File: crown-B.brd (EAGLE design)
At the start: 57.8 x 50.8 mm, 72 parts

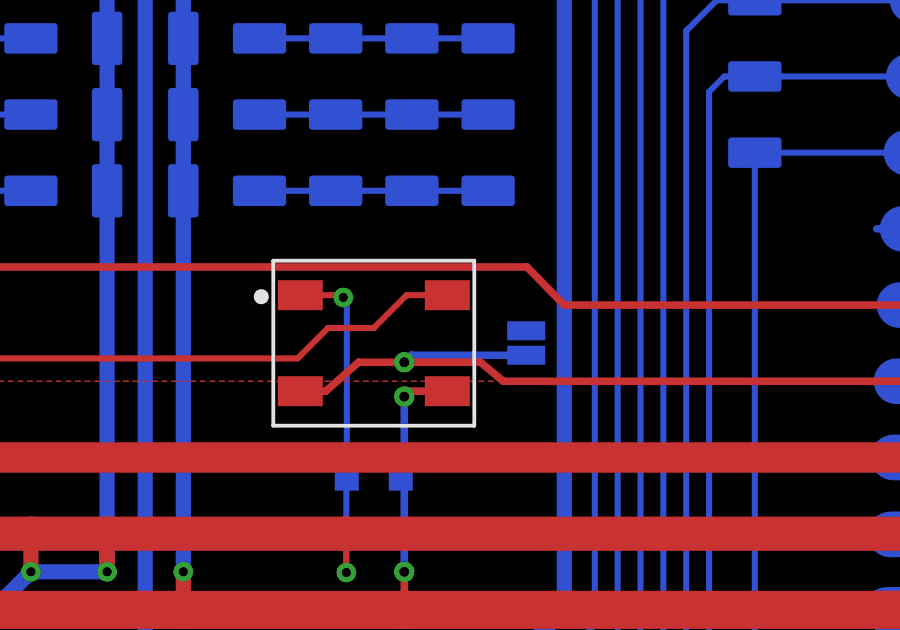
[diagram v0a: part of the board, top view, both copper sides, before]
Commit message: forgot a connection on skip-smd bits
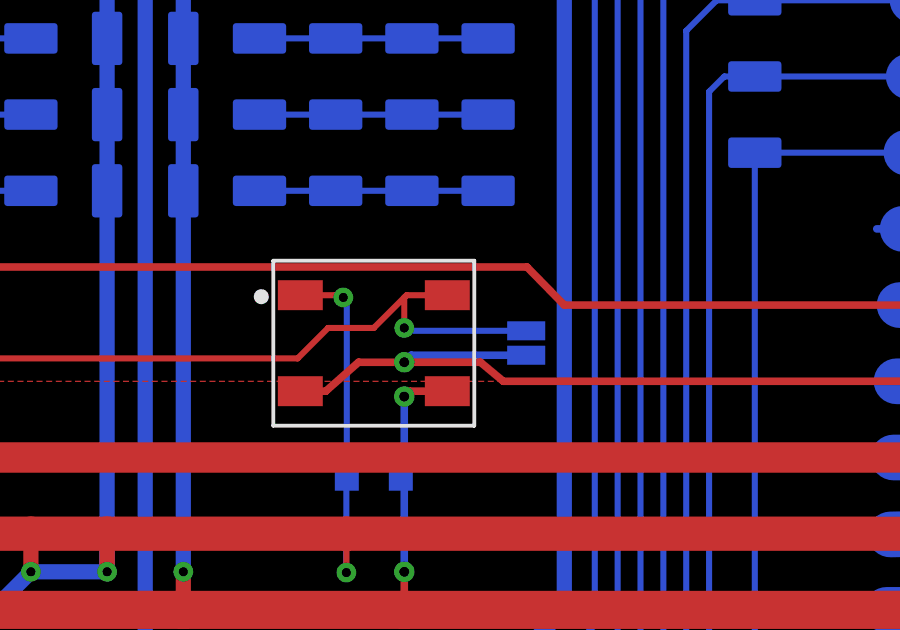
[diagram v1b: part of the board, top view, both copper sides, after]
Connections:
- net N$10: now also SKIP-SMD2.2
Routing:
- net N$10: track 28.2 -> 33.3 mm, vias 1 -> 2
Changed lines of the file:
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@@
 <grid distance="10" unitdist="mil" unit="mil" style="lines" multiple="5" display="yes" altdistance="1" altunitdist="mil" altunit="mil"/>
 <layers>
-<layer number="1" name="Top" color="4" fill="1" visible="no" active="yes"/>
-<layer number="16" name="Bottom" color="1" fill="1" visible="no" active="yes"/>
-<layer number="17" name="Pads" color="2" fill="1" visible="no" active="yes"/>
-<layer number="18" name="Vias" color="2" fill="1" visible="no" active="yes"/>
-<layer number="19" name="Unrouted" color="6" fill="1" visible="no" active="yes"/>
-<layer number="20" name="Dimension" color="15" fill="1" visible="no" active="yes"/>
-<layer number="21" name="tPlace" color="16" fill="1" visible="no" active="yes"/>
-<layer number="22" name="bPlace" color="14" fill="1" visible="no" active="yes"/>
-<layer number="23" name="tOrigins" color="15" fill="1" visible="no" active="yes"/>
-<layer number="24" name="bOrigins" color="15" fill="1" visible="no" active="yes"/>
+<layer number="1" name="Top" color="4" fill="1" visible="yes" active="yes"/>
+<layer number="16" name="Bottom" color="1" fill="1" visible="yes" active="yes"/>
+<layer number="17" name="Pads" color="2" fill="1" visible="yes" active="yes"/>
+<layer number="18" name="Vias" color="2" fill="1" visible="yes" active="yes"/>
+<layer number="19" name="Unrouted" color="6" fill="1" visible="yes" active="yes"/>
+<layer number="20" name="Dimension" color="15" fill="1" visible="yes" active="yes"/>
+<layer number="21" name="tPlace" color="16" fill="1" visible="yes" active="yes"/>
+<layer number="22" name="bPlace" color="14" fill="1" visible="yes" active="yes"/>
+<layer number="23" name="tOrigins" color="15" fill="1" visible="yes" active="yes"/>
+<layer number="24" name="bOrigins" color="15" fill="1" visible="yes" active="yes"/>
 <layer number="25" name="tNames" color="7" fill="1" visible="no" active="yes"/>
 <layer number="26" name="bNames" color="7" fill="1" visible="no" active="yes"/>
@@
 <layer number="28" name="bValues" color="7" fill="1" visible="no" active="yes"/>
 <layer number="29" name="tStop" color="7" fill="3" visible="yes" active="yes"/>
-<layer number="30" name="bStop" color="7" fill="6" visible="no" active="yes"/>
+<layer number="30" name="bStop" color="7" fill="6" visible="yes" active="yes"/>
 <layer number="31" name="tCream" color="7" fill="4" visible="no" active="yes"/>
 <layer number="32" name="bCream" color="7" fill="5" visible="no" active="yes"/>
@@
 <layer number="43" name="vRestrict" color="2" fill="10" visible="no" active="yes"/>
 <layer number="44" name="Drills" color="7" fill="1" visible="no" active="yes"/>
-<layer number="45" name="Holes" color="7" fill="1" visible="no" active="yes"/>
+<layer number="45" name="Holes" color="7" fill="1" visible="yes" active="yes"/>
 <layer number="46" name="Milling" color="3" fill="1" visible="no" active="yes"/>
 <layer number="47" name="Measures" color="7" fill="1" visible="no" active="yes"/>
@@
 <layer number="49" name="Reference" color="7" fill="1" visible="no" active="yes"/>
 <layer number="50" name="dxf" color="7" fill="1" visible="no" active="no"/>
-<layer number="51" name="tDocu" color="6" fill="1" visible="no" active="yes"/>
+<layer number="51" name="tDocu" color="6" fill="1" visible="yes" active="yes"/>
 <layer number="52" name="bDocu" color="7" fill="1" visible="no" active="yes"/>
 <layer number="53" name="tGND_GNDA" color="7" fill="9" visible="no" active="no"/>
@@
 <wire x1="35.56" y1="16.002" x2="36.576" y2="17.018" width="0.2032" layer="1"/>
 <wire x1="36.576" y1="17.018" x2="38.1" y2="17.018" width="0.2032" layer="1"/>
-<wire x1="38.1" y1="17.018" x2="39.192" y2="18.11" width="0.2032" layer="1"/>
+<wire x1="38.1" y1="17.018" x2="39.116" y2="18.034" width="0.2032" layer="1"/>
+<wire x1="39.116" y1="18.034" x2="39.192" y2="18.11" width="0.2032" layer="1"/>
 <wire x1="39.192" y1="18.11" x2="40.55" y2="18.11" width="0.2032" layer="1"/>
 <wire x1="24.892" y1="16.3631" x2="24.7849" y2="16.256" width="0.2032" layer="16"/>
@@
 <wire x1="21.336" y1="16.256" x2="21.082" y2="16.002" width="0.2032" layer="16"/>
 <via x="21.082" y="16.002" extent="1-16" drill="0.3048"/>
+<contactref element="SKIP-SMD2" pad="2"/>
+<wire x1="43.18" y1="16.9227" x2="39.2113" y2="16.9227" width="0.2032" layer="16"/>
+<wire x1="39.2113" y1="16.9227" x2="39.116" y2="17.018" width="0.2032" layer="16"/>
+<via x="39.116" y="17.018" extent="1-16" drill="0.3048"/>
+<wire x1="39.116" y1="17.018" x2="39.116" y2="18.034" width="0.2032" layer="1"/>
 </signal>
 <signal name="A0">

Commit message: fixed incorrect resistor value
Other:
- board text added: "PIXEL LINE TERMINATION (500 OHM RES)"
- board text removed: "PIXEL LINE TERMINATION (150 OHM RES)"
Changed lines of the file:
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@@
 <text x="12.954" y="16.51" size="0.762" layer="22" font="vector" ratio="15" rot="MR90" align="bottom-center">PIXEL LINE
 TERMINATION
-(150 OHM RES)</text>
+(500 OHM RES)</text>
 <text x="4.572" y="7.62" size="0.762" layer="22" font="vector" ratio="15" rot="MR0" align="center-right">GND</text>
 <text x="4.572" y="5.08" size="0.762" layer="22" font="vector" ratio="15" rot="MR0" align="center-right">VBAT</text>
